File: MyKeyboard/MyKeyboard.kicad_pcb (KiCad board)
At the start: 2 copper layers, 143.8 x 114.7 mm, 64 parts, among them J1 USB_C_Receptacle_USB2.0, J2 USB_C_Receptacle_USB2.0, J3 Conn_01x04, SW1 SW_Push, SW10 SW_Push, SW11 SW_Push, SW12 SW_Push, SW13 SW_Push, SW14 SW_Push, SW15 SW_Push, SW16 SW_Push, SW17 SW_Push, SW18 SW_Push, SW19 SW_Push, SW2 SW_Push, SW20 SW_Push, SW21 SW_Push, SW22 SW_Push, SW23 SW_Push, SW24 SW_Push, SW25 SW_Push, SW26 SW_Push, SW27 SW_Push, SW3 SW_Push, SW4 SW_Push, SW5 SW_Push, SW6 SW_Push, SW7 SW_Push, SW8 SW_Push, SW9 SW_Push, U1 E73-2G4M08S1C, U2 E73-2G4M08S1C

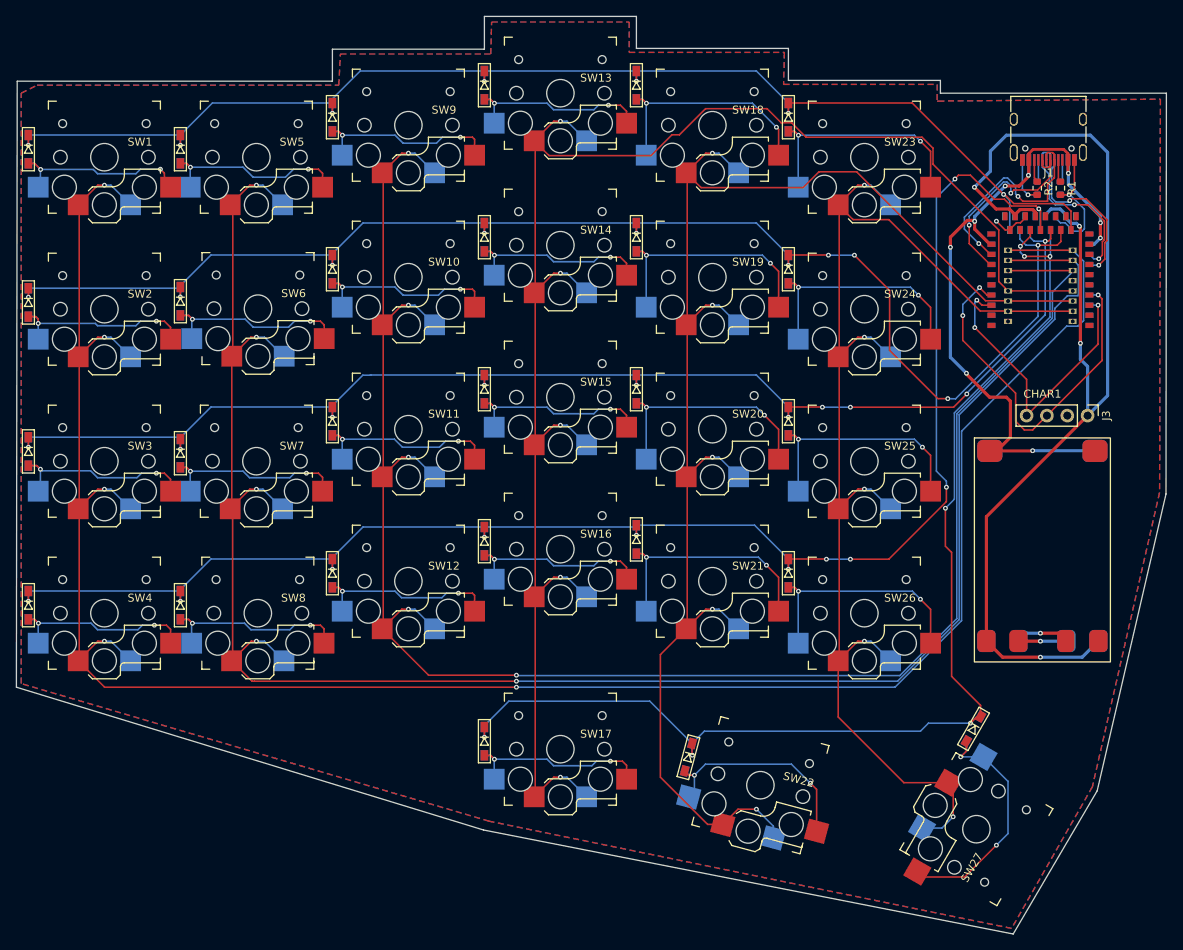
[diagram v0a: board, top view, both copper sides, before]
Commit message: update reset btn and wiring
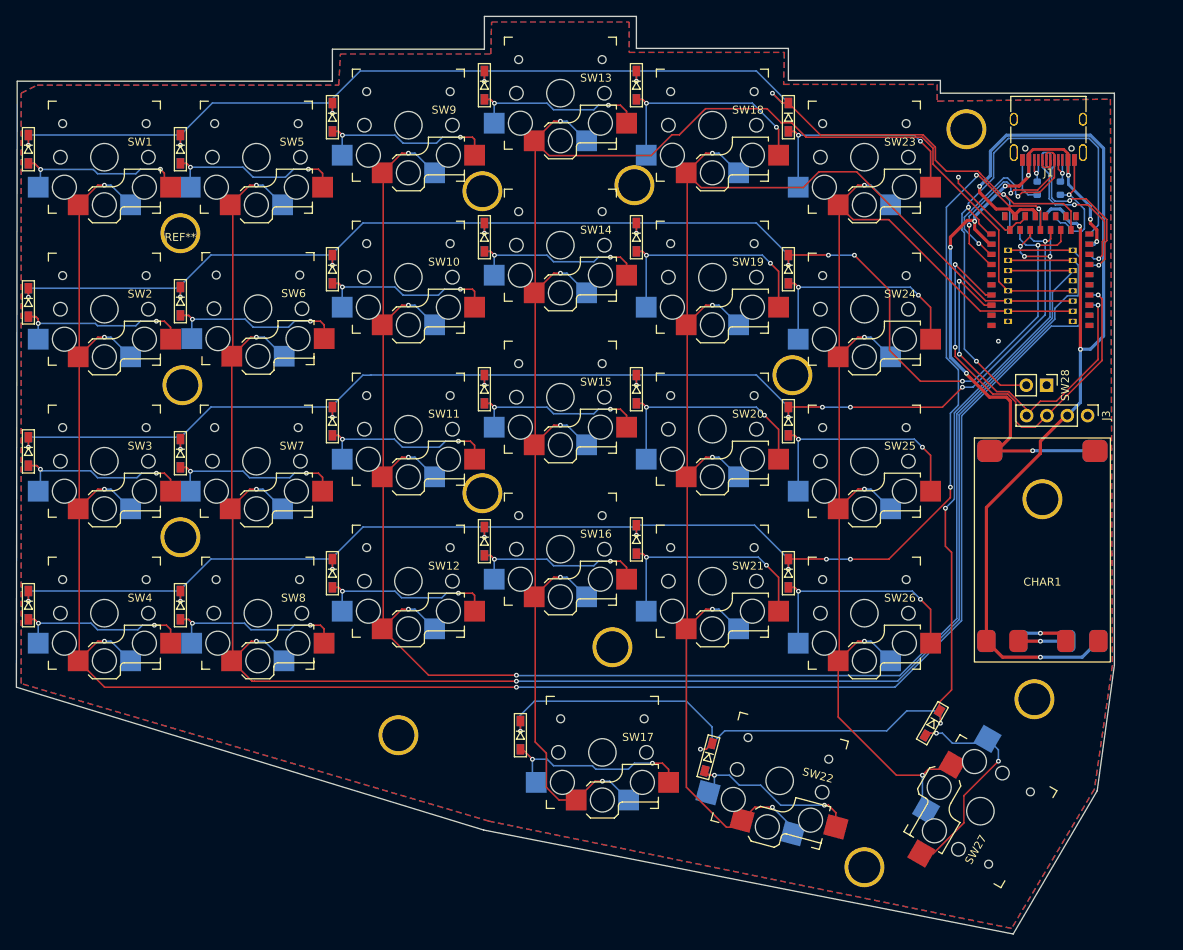
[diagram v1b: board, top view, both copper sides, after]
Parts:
- removed R1, R2: 5.1K, Resistor_SMD:R_0603_1608Metric
- added ?: , , F.Cu at (97.0, 113.5)
- added ?: , , F.Cu at (151.0, 127.2)
- added ?: , , F.Cu at (124.2, 138.2)
- added ?: , , F.Cu at (195.2, 62.5)
- added ?: , , F.Cu at (203.8, 133.8)
- added ?: , , F.Cu at (173.5, 93.2)
- added ?: , , F.Cu at (134.8, 108.0)
- added ?: , , F.Cu at (134.8, 70.2)
- added ?: , , F.Cu at (97.2, 94.5)
- added ?: , , F.Cu at (153.8, 69.5)
- added ?: , , F.Cu at (182.5, 154.8)
- added ?: , , F.Cu at (204.8, 108.8)
- added REF**: M2_Hole_TH_Outside, kbd:M2_Hole_TH_Outside, F.Cu at (97.0, 75.5)
- added SW28: SW_SPST, Connector_PinHeader_2.54mm:PinHeader_1x02_P2.54mm_Vertical, F.Cu at (205.3, 94.5)
- moved SW17 5.27 mm to (149.8, 140.4)
- moved D27 5.19 mm to (191.0, 136.8)
- moved D17 4.56 mm to (139.5, 138.2)
- moved D22 2.50 mm to (163.0, 141.0)
- moved SW22 2.47 mm to (171.9, 144.0)
- moved SW27 2.30 mm to (197.0, 147.8)
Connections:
- J1 pad B5: CC2F -> CC1B
- J2 pad B5: CC2B -> CC1F
- J3 pad 1: VCC -> GND
- J3 pad 2: GND -> VCC
- R4 pad 1: CC2B -> CC1F
- U1 pad 26: unconnected-(U1-Pad26) -> RST
- U2 pad 26: unconnected-(U2-Pad26) -> RST
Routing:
- net RST: track 0.00 -> 66.2 mm, vias 0 -> 2
- net VCC: track 145.1 -> 136.3 mm
- net SWDCLK: track 37.9 -> 46.2 mm
- net RO4: track 149.5 -> 141.9 mm
- net RWDIO: track 46.5 -> 54.0 mm
- net GND: track 28.7 -> 33.8 mm
- net Net-(D22-Pad2): track 28.3 -> 24.3 mm
- net CO5: track 159.7 -> 155.9 mm
- net CO3: track 210.2 -> 213.9 mm
- net RO0: track 163.9 -> 167.4 mm
- net CC2F: track 2.85 -> 0.00 mm
- net CC2B: track 2.83 -> 0.00 mm
- net Net-(D17-Pad2): track 24.4 -> 26.9 mm
- net Net-(D27-Pad2): track 32.1 -> 29.9 mm
- net CC1F: track 2.73 -> 4.66 mm, vias 0 -> 1
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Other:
- board size 143.8 x 114.7 mm -> 137.2 x 114.7 mm

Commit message: finalize standalone keyboard
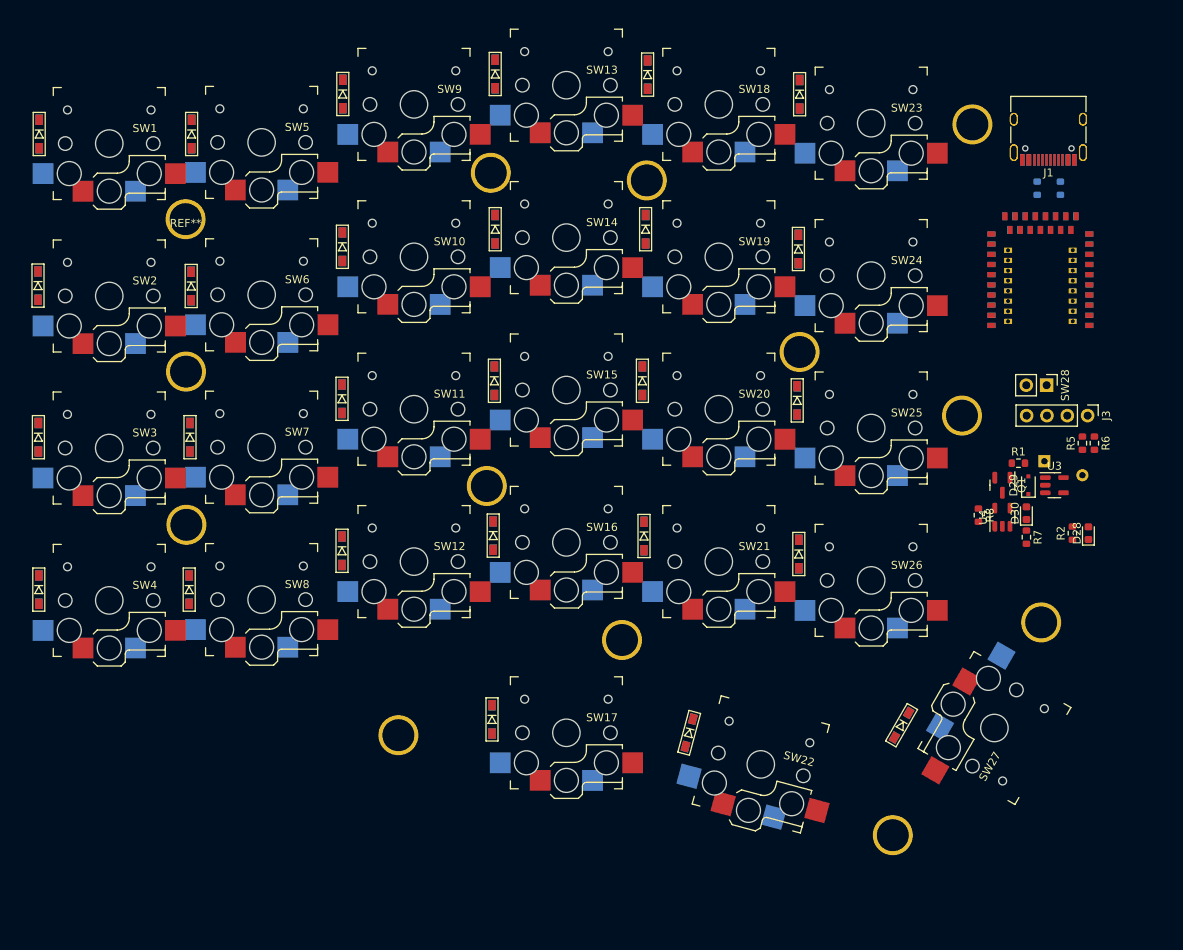
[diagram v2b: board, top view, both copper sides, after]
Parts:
- removed CHAR1: Charging_Module, Charging:4056_Charging_Type_C
- added D28: BLUE, LED_SMD:LED_0603_1608Metric, F.Cu at (210.5, 113.0)
- added D29: 1N5819, Diode_SMD:D_SOD-323F, F.Cu at (203.0, 107.0)
- added D30: RED, LED_SMD:LED_0603_1608Metric, F.Cu at (202.8, 110.5)
- added P4: GND, kbd:GND_pad, F.Cu at (209.8, 105.8)
- added P4: GND, kbd:GND_pad, F.Cu at (205.0, 104.0)
- added Q1: AO3407, Package_TO_SOT_SMD:SOT-23, F.Cu at (199.8, 107.0)
- added R1: 100K, Resistor_SMD:R_0603_1608Metric, F.Cu at (201.8, 104.2)
- added R2: 1K, Resistor_SMD:R_0603_1608Metric, F.Cu at (208.5, 113.0)
- added R5: 820K, Resistor_SMD:R_0603_1608Metric, F.Cu at (209.8, 101.8)
- added R6: 2M, Resistor_SMD:R_0603_1608Metric, F.Cu at (211.2, 101.8)
- added R7: 1K, Resistor_SMD:R_0603_1608Metric, F.Cu at (202.8, 113.5)
- added R8: RPROG, Resistor_SMD:R_0603_1608Metric, F.Cu at (196.8, 110.8)
- added U3: AP2112K-3.3, Package_TO_SOT_SMD:SOT-23-5, F.Cu at (206.2, 107.0)
- added U4: TP4054, Package_TO_SOT_SMD:SOT-23-5, F.Cu at (199.8, 111.0)
- moved ? 14.5 mm to (194.7, 98.3)
- moved SW27 10.5 mm to (198.8, 137.3)
- moved ? 9.64 mm to (204.6, 124.2)
- moved ? 5.35 mm to (186.1, 150.8)
- moved SW17 5.12 mm to (145.2, 137.9)
- moved SW23 4.33 mm to (183.3, 61.8)
- moved SW24 4.29 mm to (183.3, 80.8)
- moved SW25 4.24 mm to (183.3, 99.8)
- moved SW26 4.19 mm to (183.3, 118.9)
- moved D17 4.06 mm to (135.9, 136.3)
- moved D22 3.88 mm to (160.6, 137.9)
- moved D27 3.86 mm to (187.2, 137.0)
- moved D23 3.20 mm to (174.4, 58.1)
- moved D9 3.18 mm to (117.3, 58.1)
- moved SW22 3.13 mm to (169.5, 141.9)
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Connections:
- net VBUSB renamed VBUS
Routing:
- net CO0: track 269.8 -> 0.00 mm, vias 5 -> 0
- net CO1: track 246.9 -> 0.00 mm, vias 5 -> 0
- net CO2: track 226.5 -> 0.00 mm, vias 5 -> 0
- net CO3: track 213.9 -> 0.00 mm, vias 5 -> 0
- net RO3: track 197.0 -> 0.00 mm, vias 11 -> 0
- net CO4: track 186.2 -> 0.00 mm, vias 5 -> 0
- net RO1: track 177.8 -> 0.00 mm, vias 10 -> 0
- net RO0: track 167.4 -> 0.00 mm, vias 7 -> 0
- net RO2: track 167.1 -> 0.00 mm, vias 10 -> 0
- net CO5: track 155.9 -> 0.00 mm, vias 5 -> 0
- net RO4: track 141.9 -> 0.00 mm, vias 7 -> 0
- net VCC: track 136.3 -> 0.00 mm, vias 4 -> 0
- net VBUS: track 88.7 -> 0.00 mm, vias 9 -> 0
- net RST: track 66.2 -> 0.00 mm, vias 2 -> 0
- net RWDIO: track 54.0 -> 0.00 mm, vias 3 -> 0
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- removed copper zone on B.Cu, net GND
- removed copper zone on F.Cu, net GND
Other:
- board outline removed
